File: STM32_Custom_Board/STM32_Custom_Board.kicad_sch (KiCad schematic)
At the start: 28 parts, among them J1 USB_B_Micro, J2 Conn_01x04_Male, J3 Conn_01x04_Male, J4 Conn_01x04_Male, SW1 SW_SPDT, U1 AMS1117-3.3, U2 STM32F103C8T6, Y1 16MHz

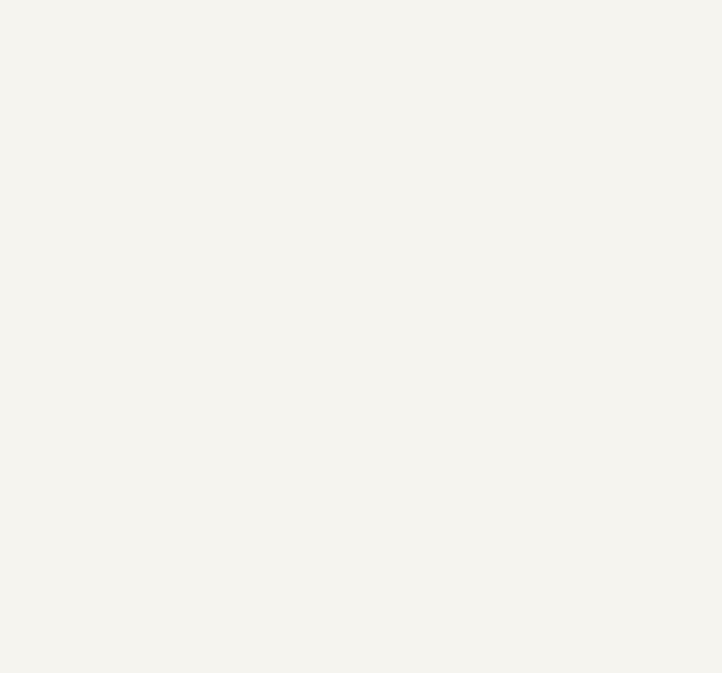
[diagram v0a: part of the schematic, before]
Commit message: Board outline finished and connectors put in place
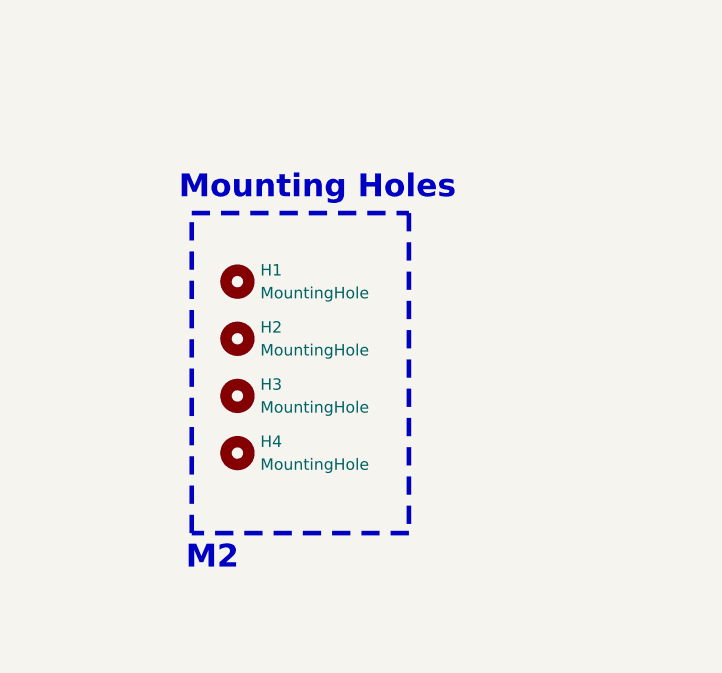
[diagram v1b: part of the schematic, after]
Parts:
- added H1, H2, H3, H4: MountingHole, MountingHole:MountingHole_2.1mm, symbol Mechanical:MountingHole
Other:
- note added: "M2"
- note added: "Mounting Holes"

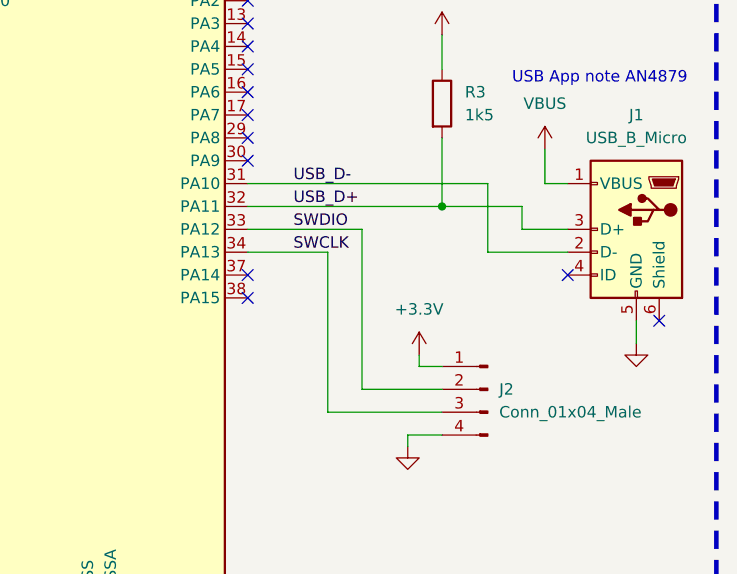
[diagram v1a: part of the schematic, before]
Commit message: Routing of signals finished
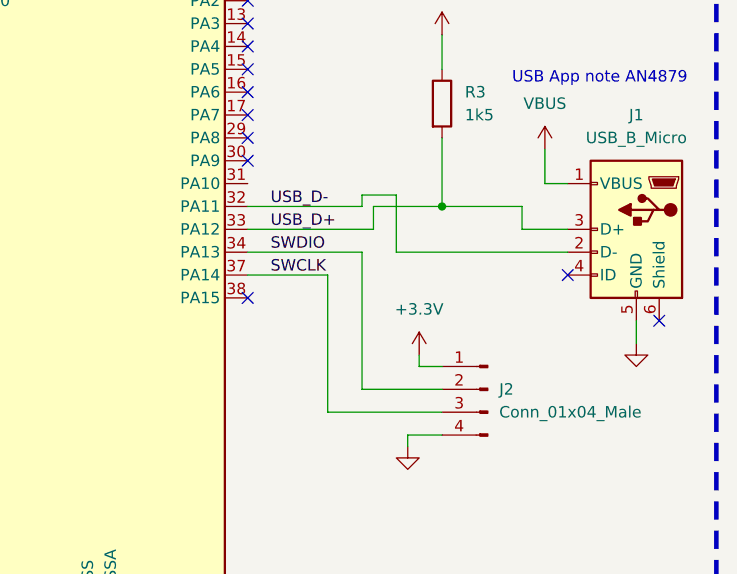
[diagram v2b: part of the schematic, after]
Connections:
- net SWCLK: now also U2.37 (PA14); no longer U2.34 (PA13)
- net SWDIO: now also U2.34 (PA13); no longer U2.33 (PA12)
- net USB_D+: now also U2.33 (PA12); no longer U2.32 (PA11)
- net USB_D-: now also U2.32 (PA11); no longer U2.31 (PA10)
- no-connect marks 29 -> 28
